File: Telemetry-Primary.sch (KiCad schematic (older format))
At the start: 43 parts, among them J2 PWRConn, J3 Micro_SD_Card_Det, J4 CANConn_OUT, J5 CANConn_IN, J6 Conn_02x08_Odd_Even, J7 Conn_02x15_Odd_Even, J8 Conn_02x10_Odd_Even, J9 Conn_02x17_Odd_Even, U2 ADM3055E, U3 PQMC3-Dx-Sx-S, U4 CDSOT23-T24CAN

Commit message: Adds new telemetry board schematics. Still need to place GPS and Ethernet and some main uC essentials
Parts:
- removed C1, C4, C9: .1u, Capacitor_SMD:C_0805_2012Metric, symbol Device:C
- removed C10, C2: .01u, Capacitor_SMD:C_0805_2012Metric, symbol Device:C
- removed C11, C3, C8: 10u, Capacitor_SMD:C_0805_2012Metric, symbol Device:C
- removed C12, C5: 100u, Capacitor_SMD:C_0805_2012Metric, symbol Device:C
- removed C6: 47u, Capacitor_SMD:C_0805_2012Metric, symbol Device:C
- removed C7: .22u, Capacitor_SMD:C_0805_2012Metric, symbol Device:C
- removed D1: LED, LED_SMD:LED_0805_2012Metric, symbol Device:LED
- removed J2: PWRConn, Connector_Molex:Molex_Micro-Fit_3.0_43650-0215_1x02_P3.00mm_Vertical, symbol Connector_Generic:Conn_01x02
- removed J3: Micro_SD_Card_Det, Connector_Card:microSD_HC_Hirose_DM3AT-SF-PEJM5, symbol Connector:Micro_SD_Card_Det
- removed J4: CANConn_OUT, Connector_Molex:Molex_Micro-Fit_3.0_43650-0415_1x04_P3.00mm_Vertical, symbol Connector_Generic:Conn_01x04
- removed J5: CANConn_IN, Connector_Molex:Molex_Micro-Fit_3.0_43650-0415_1x04_P3.00mm_Vertical, symbol Connector_Generic:Conn_01x04
- removed JP1: Jumper, Connector_PinHeader_2.54mm:PinHeader_1x02_P2.54mm_Vertical, symbol Device:Jumper
- removed L1: 5u, Inductor_SMD:L_TDK_NLV32_3.2x2.5mm, symbol Device:L
- removed L2, L3: 2k, Inductor_SMD:L_0805_2012Metric, symbol Device:L
- removed R1: 0, Resistor_SMD:R_0805_2012Metric, symbol Device:R
- removed R2: 120, Resistor_SMD:R_0805_2012Metric, symbol Device:R
- removed R3: 3k, Resistor_SMD:R_0805_2012Metric, symbol Device:R
- removed TP1: CAN_TD, TestPoint:TestPoint_Keystone_5005-5009_Compact, symbol Connector:TestPoint
- removed TP10: CAN_L, TestPoint:TestPoint_Keystone_5005-5009_Compact, symbol Connector:TestPoint
- removed TP13: 9VIN, TestPoint:TestPoint_Keystone_5005-5009_Compact, symbol Connector:TestPoint
- removed TP14: 9V_GND, TestPoint:TestPoint_Keystone_5005-5009_Compact, symbol Connector:TestPoint
- removed TP2: CAN_RD, TestPoint:TestPoint_Keystone_5005-5009_Compact, symbol Connector:TestPoint
- removed TP3: 12VIN, TestPoint:TestPoint_Keystone_5005-5009_Compact, symbol Connector:TestPoint
- removed TP4: 12V_GND, TestPoint:TestPoint_Keystone_5005-5009_Compact, symbol Connector:TestPoint
- removed TP5: CAN_ISO_VIN, TestPoint:TestPoint_Keystone_5005-5009_Compact, symbol Connector:TestPoint
- removed TP6: CAN_ISO_VOUT, TestPoint:TestPoint_Keystone_5005-5009_Compact, symbol Connector:TestPoint
- removed TP7: CAN_ISO_GNDIN, TestPoint:TestPoint_Keystone_5005-5009_Compact, symbol Connector:TestPoint
- removed TP8: CAN_ISO_GNDOUT, TestPoint:TestPoint_Keystone_5005-5009_Compact, symbol Connector:TestPoint
- removed TP9: CAN_H, TestPoint:TestPoint_Keystone_5005-5009_Compact, symbol Connector:TestPoint
- removed U2: ADM3055E, UTSVT_ICs:SOIC-20W_7.5x15.4mm_Pitch1.27mm, symbol utsvt-chips:ADM3055E
- removed U3: PQMC3-Dx-Sx-S, UTSVT_ICs:CUI_PQMC3-S, symbol utsvt-power-regulators:PQMC3-Dx-Sx-S
- removed U4: CDSOT23-T24CAN, Package_TO_SOT_SMD:SOT-23W_Handsoldering, symbol utsvt-chips:CDSOT23-T24CAN
- added C? (x9): 0.1u, Capacitor_SMD:C_0805_2012Metri, symbol Device:C_Small
- added C?: 1u, Capacitor_SMD:C_0805_2012Metri, symbol Device:C_Small
- added C?: 4.7u, Capacitor_SMD:C_0805_2012Metri, symbol Device:C_Small
- added J?: SWD, Connector_PinHeader_2.54mm:PinHeader_1x04_P2.54mm_Vertical, symbol Connector_Generic:Conn_01x04
- added U?: STM32F429VITx, Package_QFP:LQFP-100_14x14mm_P0.5mm, symbol MCU_ST_STM32F4:STM32F429VITx
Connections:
- net labels added: NRST, SWCLK, SWDIO
- net labels removed: +12V, GNDPWR, VDD
- wire segments 156 -> 94
- no-connect marks 96 -> 88
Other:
- note added: "Addr: 0x28"
- note added: "Addr: 0x68"
- note added: "Isolated +5V and +3.3V.\nUse GND as local gnd for all board electronic components.\nConnect GNDPWR when using +12V."
- note added: "One 0.1u cap per VDD pin. Place 4.7u near any VDD pin."
- note added: "Place near pin 22"
- note added: "Use 0.1uF instead of 2.2u because\ninternal voltage regulator is not used."
- note added: "VDD/VSS"
- note added: "VDDA/VSSA"
- note added: "uC Tx -> CAN Tx\nuC Rx -> CAN Rx"
- note added: "uC Tx -> UART Rx\nuC Rx -> UART Tx"

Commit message: Updates common component library
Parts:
- removed C? (x2): 0.1u, Capacitor_SMD:C_0805_2012Metri, symbol Device:C_Small
- removed J6: Conn_02x08_Odd_Even, Connector_PinHeader_2.54mm:PinHeader_2x08_P2.54mm_Vertical, symbol Connector_Generic:Conn_02x08_Odd_Even
- removed J7: Conn_02x15_Odd_Even, Connector_PinHeader_2.54mm:PinHeader_2x15_P2.54mm_Vertical, symbol Connector_Generic:Conn_02x15_Odd_Even
- removed J8: Conn_02x10_Odd_Even, Connector_PinHeader_2.54mm:PinHeader_2x10_P2.54mm_Vertical, symbol Connector_Generic:Conn_02x10_Odd_Even
- removed J9: Conn_02x17_Odd_Even, Connector_PinHeader_2.54mm:PinHeader_2x17_P2.54mm_Vertical, symbol Connector_Generic:Conn_02x17_Odd_Even
- removed U?: STM32F429VITx, Package_QFP:LQFP-100_14x14mm_P0.5mm, symbol MCU_ST_STM32F4:STM32F429VITx
- added C? (x9): 0.1u, Capacitor_SMD:C_0805_2012Metri, symbol Device:C_Small
- added C? (x2): 18p, Capacitor_SMD:C_0805_2012Metri, symbol Device:C_Small
- added H? (x4): M.3, MountingHole:MountingHole_3mm, symbol Mechanical:MountingHole
- added LOGO?: Dr. Hallock, UTSVT_Special:Hallock_Image, symbol utsvt-misc:Logo_Placeholder
- added LOGO?: UTSVT Logo, UTSVT_Special:UTSVT_Logo_Symbol, symbol utsvt-misc:Logo_Placeholder
- added SW?: SW_Push, symbol Switch:SW_Push
- added U?: STM32F429ZITx, Package_QFP:LQFP-144_20x20mm_P0.5mm, symbol MCU_ST_STM32F4:STM32F429ZITx
- added Y?: 8M, Crystal:Crystal_SMD_TXC_7A-2Pin_5x3.2mm, symbol Device:Crystal_Small
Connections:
- net labels removed: +9V, CAN_RD, CAN_TD, CLOCK, CS, DET, MISO, MOSI
- wire segments 94 -> 155
- no-connect marks 88 -> 0
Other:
- note added: "Graphics/Logos"
- note added: "STM32 Essentials"
- moved on the sheet: C?, J?

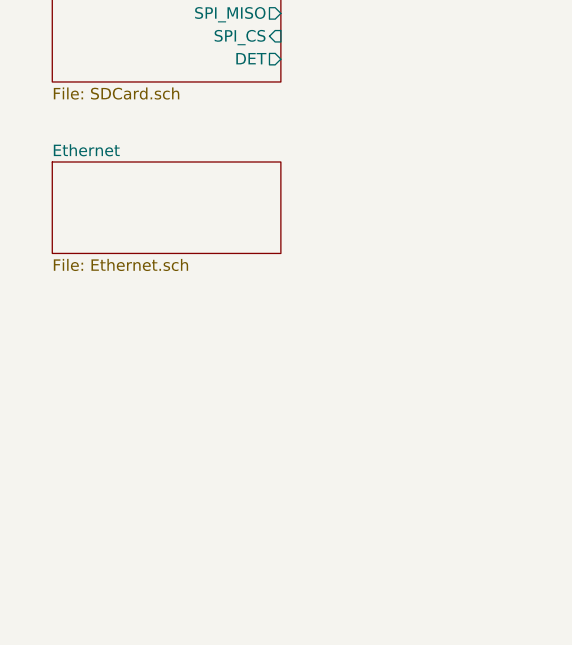
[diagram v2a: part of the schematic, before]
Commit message: Adds GPS module to common library
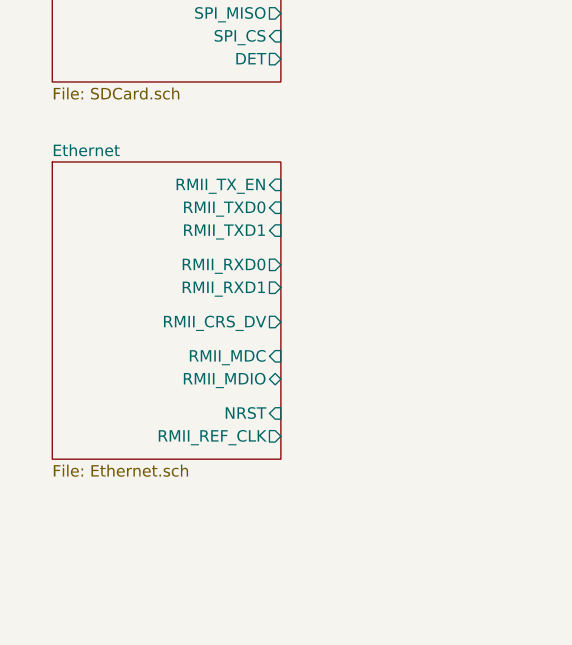
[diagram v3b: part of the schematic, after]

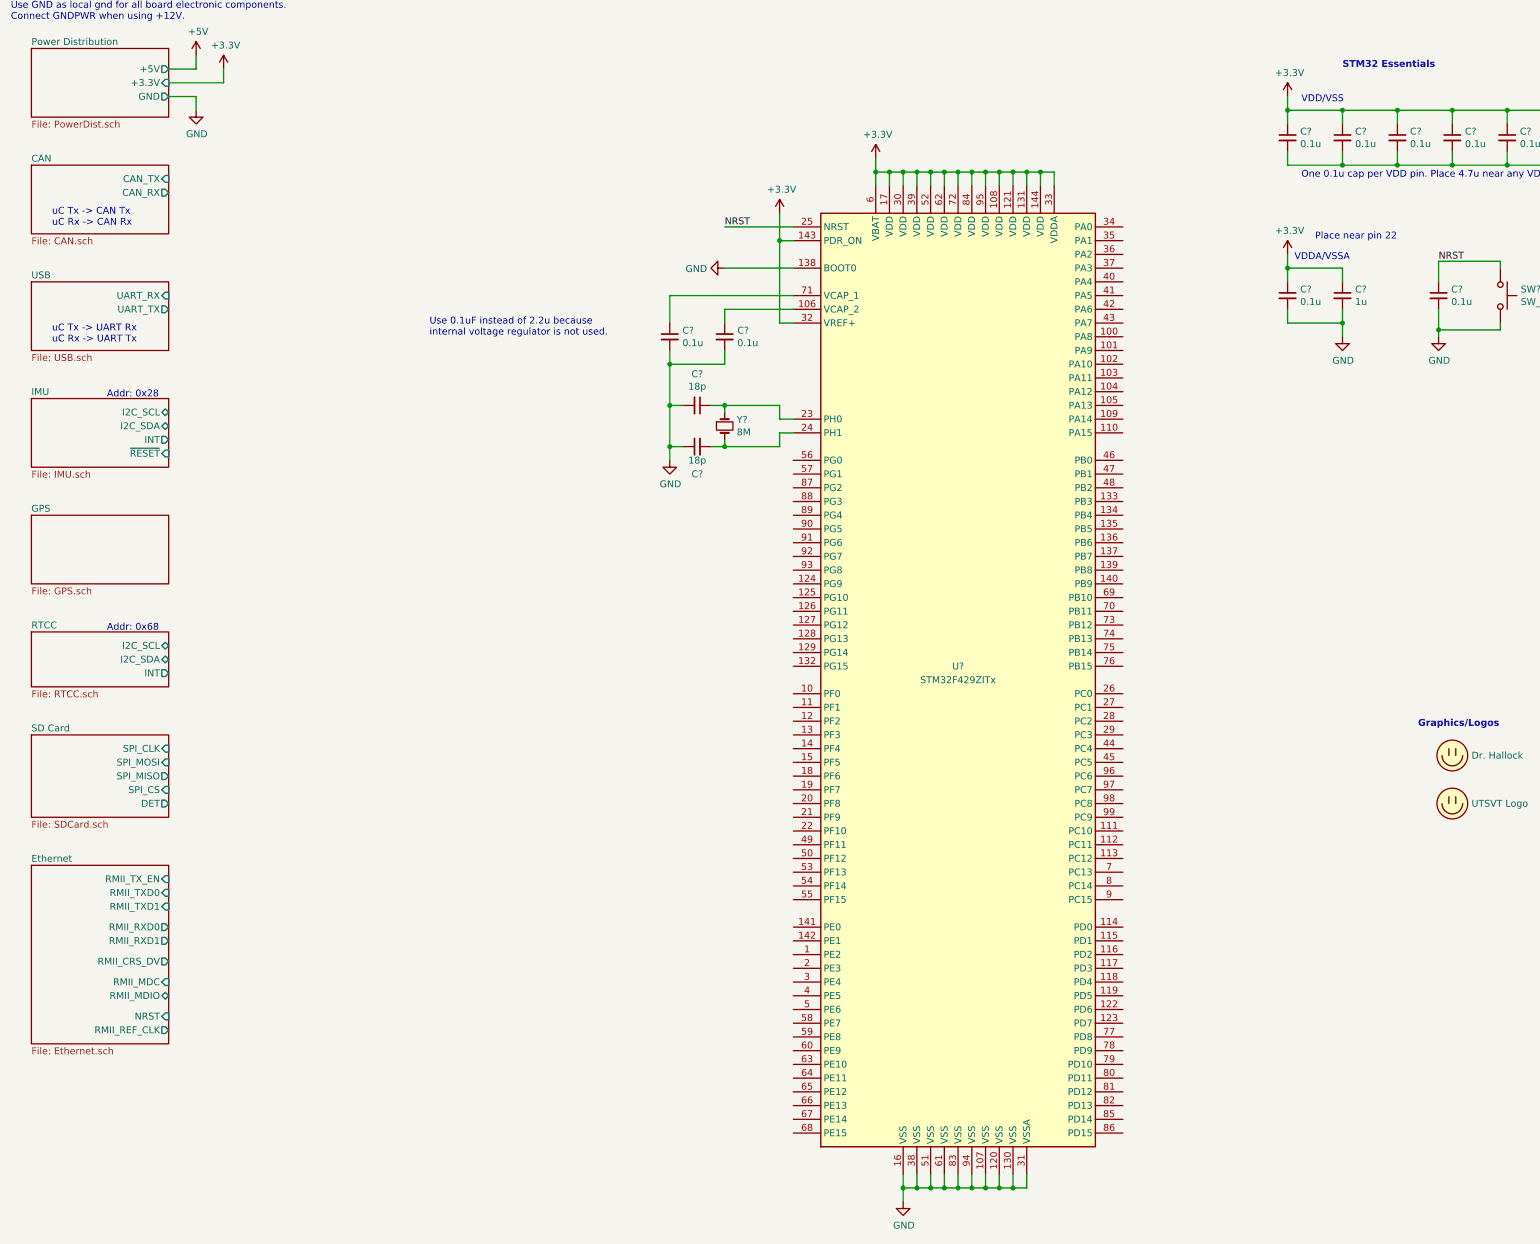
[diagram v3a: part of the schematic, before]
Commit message: Adds connects all modules except for LEDs in schematics
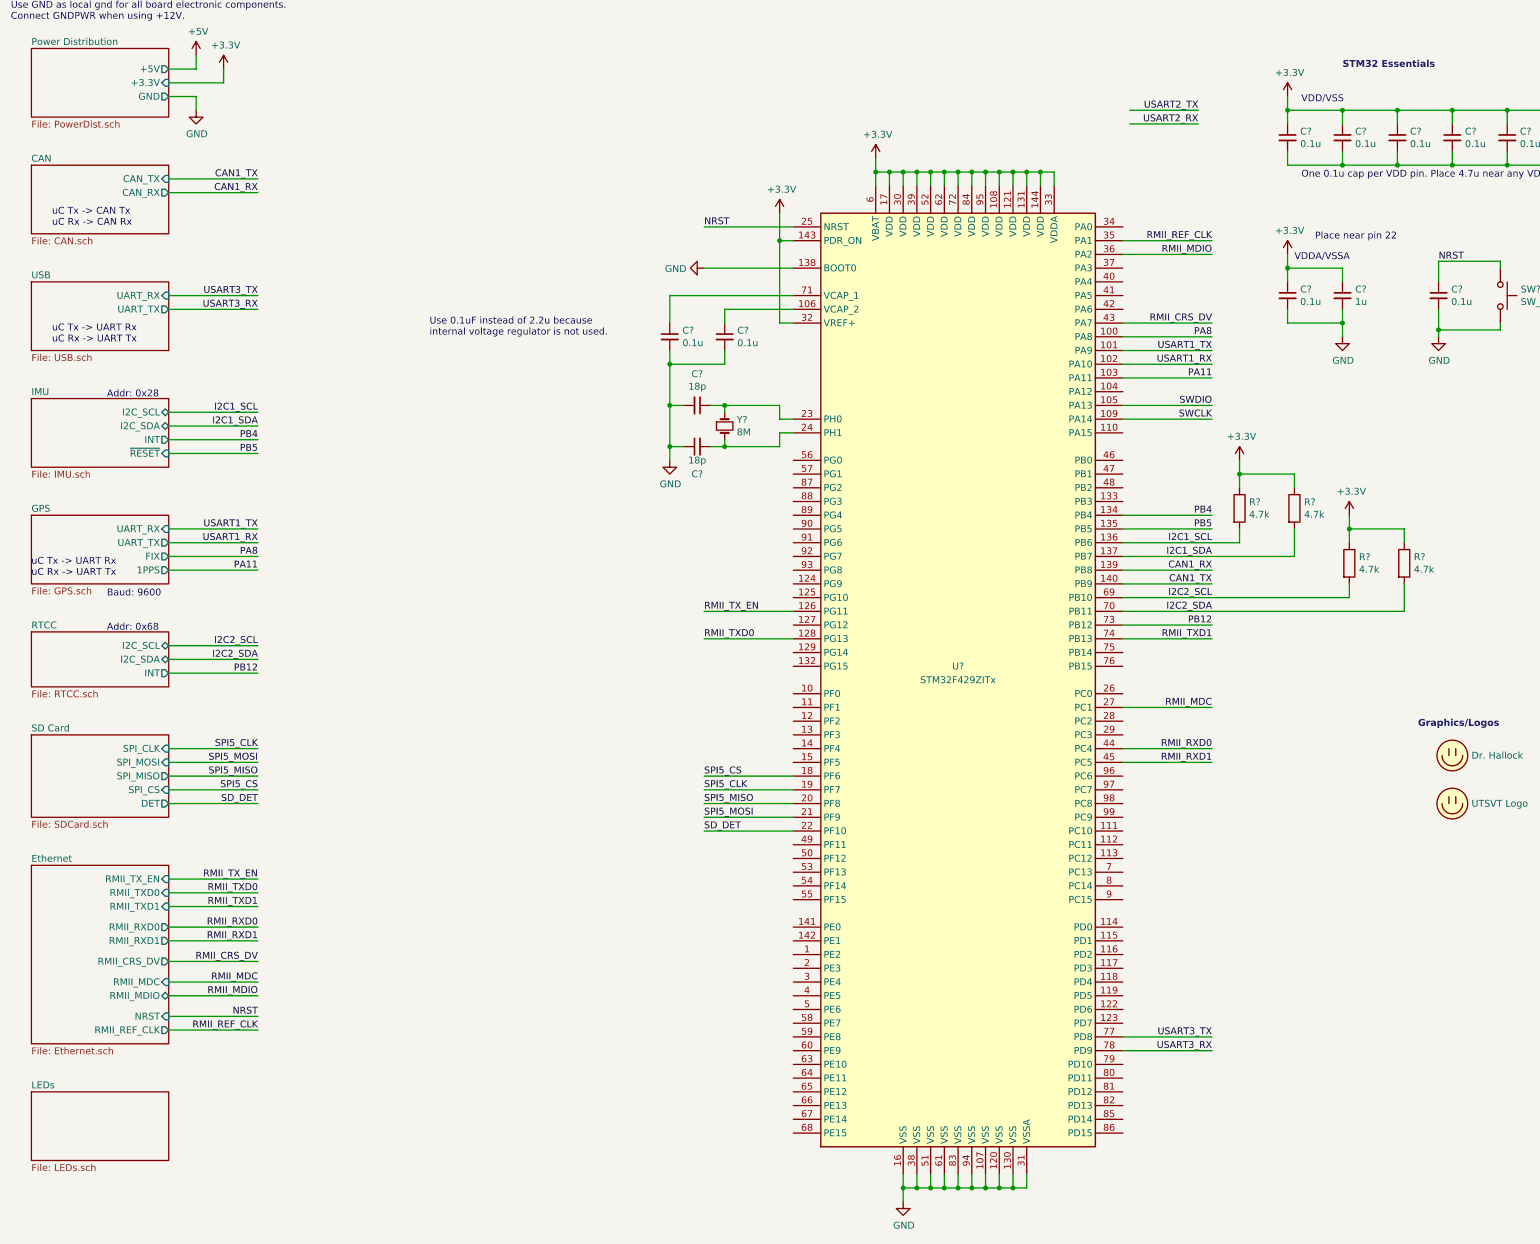
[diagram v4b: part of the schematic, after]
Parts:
- added R? (x4): 4.7k, Resistor_SMD:R_0805_2012Metric, symbol Device:R
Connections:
- net +3V3: now also R?.1, R?.1, R?.1, R?.1
- net SWCLK: now also U?.109 (PA14)
- net SWDIO: now also U?.105 (PA13)
- net PA8: now reaches U?.100 (PA8)
- net USART1_TX: now reaches U?.101 (PA9)
- net USART1_RX: now reaches U?.102 (PA10)
- net PA11: now reaches U?.103 (PA11)
- net RMII_TX_EN: now reaches U?.126 (PG11)
- net RMII_TXD0: now reaches U?.128 (PG13)
- net PB4: now reaches U?.134 (PB4)
- net PB5: now reaches U?.135 (PB5)
- net I2C1_SCL: now reaches U?.136 (PB6)
- net I2C1_SCL: now also R?.2
- net I2C1_SDA: now reaches U?.137 (PB7)
- net I2C1_SDA: now also R?.2
- net CAN1_RX: now reaches U?.139 (PB8)
- net CAN1_TX: now reaches U?.140 (PB9)
- net SPI5_CS: now reaches U?.18 (PF6)
- net SPI5_CLK: now reaches U?.19 (PF7)
- net SPI5_MISO: now reaches U?.20 (PF8)
- net SPI5_MOSI: now reaches U?.21 (PF9)
- net SD_DET: now reaches U?.22 (PF10)
- net RMII_MDC: now reaches U?.27 (PC1)
- net RMII_REF_CLK: now reaches U?.35 (PA1)
- net RMII_MDIO: now reaches U?.36 (PA2)
- net RMII_CRS_DV: now reaches U?.43 (PA7)
- net RMII_RXD0: now reaches U?.44 (PC4)
- net RMII_RXD1: now reaches U?.45 (PC5)
- net I2C2_SCL: now reaches U?.69 (PB10)
- net I2C2_SCL: now also R?.2
- net I2C2_SDA: now reaches U?.70 (PB11)
- net I2C2_SDA: now also R?.2
- net PB12: now reaches U?.73 (PB12)
- net RMII_TXD1: now reaches U?.74 (PB13)
- net USART3_TX: now reaches U?.77 (PD8)
- net USART3_RX: now reaches U?.78 (PD9)
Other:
- note added: "Baud: 9600"
